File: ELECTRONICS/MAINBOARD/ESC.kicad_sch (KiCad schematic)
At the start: 3 parts, among them U13 STM32G031C6Tx

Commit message: Add files via upload
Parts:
- added J5, J6: Conn_01x05_Socket, Connector_PinHeader_2.54mm:PinHeader_1x05_P2.54mm_Vertical, symbol Connector:Conn_01x05_Socket
- added J7: Conn_01x02_Pin, symbol Connector:Conn_01x02_Pin
- renumbered C35 to C36, C36 to C37, U13 to U17
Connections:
- net +3V3: now also J5.2 (Pin_2), J6.2 (Pin_2)
- net GNDREF: now also J5.3 (Pin_3), J6.3 (Pin_3), J7.2 (Pin_2)
- net MCT8316Z/BRAKE: now also U17.43 (PB4)
- net MCT8316Z/DRVOFF: now also U17.44 (PB5)
- net MCT8316Z/nSCS: now also U17.48 (PB9)
- net AMT_A_R: now reaches U17.11 (PA0)
- net AMT_B_R: now reaches U17.12 (PA1)
- net MCT8316Z1/SDI: now reaches U17.13 (PA2)
- net AMT_X_L: now reaches U17.14 (PA3)
- net MCT8316Z1/nSCS: now reaches U17.15 (PA4)
- net MCT8316Z1/SCLK: now reaches U17.16 (PA5)
- net MCT8316Z1/SDO: now reaches U17.17 (PA6)
- net MCT8316Z1/nSLEEP: now reaches U17.18 (PA7)
- net nFAULT_R: now reaches U17.19 (PB0)
- net FGOUT_R: now reaches U17.20 (PB1)
- net DRVOFF_R: now reaches U17.21 (PB2)
- net BRAKE_R: now reaches U17.22 (PB10)
- net AMT_X_R: now reaches U17.27 (PB15)
- net MCT8316Z1/PWM: now reaches U17.28 (PA8)
- net USART_TX: now reaches U17.29 (USART1_TX/PA9)
- net AMT_A_L: now reaches U17.30 (PC6)
- net AMT_B_L: now reaches U17.31 (PC7)
- net USART_RX: now reaches U17.32 (USART1_RX/PA10)
- net SWDIO: now reaches U17.35 (PA13)
- net SWDIO: now also J6.4 (Pin_4)
- net SWCLK: now reaches U17.36 (PA14)
- net SWCLK: now also J6.5 (Pin_5)
- net FGOUT_L: now reaches U17.39 (PD1)
- net nFAULT_L: now reaches U17.40 (PD2)
- net nSLEEP_L: now reaches U17.41 (PD3)
- net MCT_L_PWM: now reaches U17.42 (PB3)
- net MCT8316Z/SDI: now reaches U17.45 (PB6)
- net MCT8316Z/SDO: now reaches U17.46 (PB7)
- net MCT8316Z/SCLK: now reaches U17.47 (PB8)
- net PF0 renamed nRESET
- new net +24V: J7.1 (Pin_1)
- new net NRESET: J5.5 (Pin_5)
- no-connect marks 0 -> 11
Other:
- sheet MCT8316Z ports: added SCLK, SDI, SDO; removed none
- sheet MCT8316Z1 ports: added 24V, BRAKE, DRVOFF, FGOUT, PWM, SCLK, SDI, SDO, nFAULT, nSCS, nSLEEP; removed none
- note added: "SWIM NC"

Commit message: Add files via upload
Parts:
- removed J7: Conn_01x02_Pin, symbol Connector:Conn_01x02_Pin
- added J4: Conn_01x02_Socket, symbol Connector:Conn_01x02_Socket
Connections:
- net USART_RX: now also J4.1 (Pin_1)
- net USART_TX: now also J4.2 (Pin_2)
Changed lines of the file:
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@@
-	)
-	(junction
-		(at 198.12 26.67)
-		(diameter 0)
-		(color 0 0 0 0)
 	)
 	(junction
@@
 	(wire
 		(pts
-			(xy 171.45 29.21) (xy 168.91 29.21)
-		)
-		(stroke
-			(width 0)
-			(type default)
-		)
-	)
-	(wire
-		(pts
 			(xy 149.86 93.98) (xy 161.29 93.98)
 		)
@@
 	(wire
 		(pts
+			(xy 78.74 83.82) (xy 78.74 87.63)
+		)
+		(stroke
+			(width 0)
+			(type default)
+		)
+	)
+	(wire
+		(pts
 			(xy 107.95 55.88) (xy 114.3 55.88)
 		)
@@
 	(wire
 		(pts
+			(xy 78.74 93.98) (xy 88.9 93.98)
+		)
+		(stroke
+			(width 0)
+			(type default)
+		)
+	)
+	(wire
+		(pts
 			(xy 149.86 99.06) (xy 162.56 99.06)
 		)
@@
 	(wire
 		(pts
+			(xy 78.74 83.82) (xy 88.9 83.82)
+		)
+		(stroke
+			(width 0)
+			(type default)
+		)
+	)
+	(wire
+		(pts
 			(xy 149.86 96.52) (xy 162.56 96.52)
 		)
@@
 	(wire
 		(pts
+			(xy 72.39 90.17) (xy 78.74 90.17)
+		)
+		(stroke
+			(width 0)
+			(type default)
+		)
+	)
+	(wire
+		(pts
 			(xy 149.86 68.58) (xy 162.56 68.58)
 		)
@@
 	(wire
 		(pts
+			(xy 78.74 93.98) (xy 78.74 90.17)
+		)
+		(stroke
+			(width 0)
+			(type default)
+		)
+	)
+	(wire
+		(pts
 			(xy 180.34 63.5) (xy 189.23 63.5)
 		)
@@
 	(wire
 		(pts
-			(xy 168.91 26.67) (xy 198.12 26.67)
+			(xy 78.74 87.63) (xy 72.39 87.63)
 		)
 		(stroke
@@
 		)
 	)
+	(label "USART_RX"
+		(at 88.9 93.98 180)
+		(effects
+			(font
+				(size 1.27 1.27)
+			)
+			(justify right bottom)
+		)
+	)
 	(label "nRESET"
 		(at 105.41 58.42 0)
@@
 		)
 	)
-	(label "PWM_L"
+	(label "MCT_L_PWM"
 		(at 190.5 101.6 180)
 		(effects
@@
 	(label "USART_TX"
 		(at 161.29 71.12 180)
+		(effects
+			(font
+				(size 1.27 1.27)
+			)
+			(justify right bottom)
+		)
+	)
+	(label "USART_TX"
+		(at 88.9 83.82 180)
 		(effects
 			(font
@@
 		)
 	)
+	(hierarchical_label "USART_RX"
+		(shape input)
+		(at 78.74 90.17 0)
+		(effects
+			(font
+				(size 1.27 1.27)
+			)
+			(justify left)
+		)
+	)
 	(hierarchical_label "AMT_B_L"
 		(shape output)
@@
 			)
 			(justify left)
+		)
+	)
+	(hierarchical_label "USART_TX"
+		(shape output)
+		(at 78.74 87.63 0)
+		(effects
+			(font
+				(size 1.27 1.27)
+			)
+			(justify left)
+		)
+	)
+	(hierarchical_label "24V"
+		(shape input)
+		(at 198.12 26.67 180)
+		(effects
+			(font
+				(size 1.27 1.27)
+			)
+			(justify right)
 		)
 	)
@@
 	)
 	(symbol
-		(lib_id "Connector:Conn_01x02_Pin")
-		(at 163.83 26.67 0)
-		(unit 1)
-		(body_style 1)
-		(exclude_from_sim no)
-		(in_bom yes)
-		(on_board yes)
-		(in_pos_files yes)
-		(dnp no)
-		(fields_autoplaced yes)
-		(property "Reference" "J7"
-			(at 164.465 21.59 0)
-			(show_name no)
-			(do_not_autoplace no)
-			(effects
-				(font
-					(size 1.27 1.27)
-				)
-			)
-		)
-		(property "Value" "Conn_01x02_Pin"
-			(at 164.465 24.13 0)
-			(show_name no)
-			(do_not_autoplace no)
-			(effects
-				(font
-					(size 1.27 1.27)
-				)
-			)
-		)
-		(property "Footprint" ""
-			(at 163.83 26.67 0)
-			(hide yes)
-			(show_name no)
-			(do_not_autoplace no)
-			(effects
-				(font
-					(size 1.27 1.27)
-				)
-			)
-		)
-		(property "Datasheet" ""
-			(at 163.83 26.67 0)
-			(hide yes)
-			(show_name no)
-			(do_not_autoplace no)
-			(effects
-				(font
-					(size 1.27 1.27)
-				)
-			)
-		)
-		(property "Description" "Generic connector, single row, 01x02, script generated"
-			(at 163.83 26.67 0)
-			(hide yes)
-			(show_name no)
-			(do_not_autoplace no)
-			(effects
-				(font
-					(size 1.27 1.27)
-				)
-			)
-		)
-		(pin "1"
-		)
-		(pin "2"
-		)
-		(instances
-			(project "autobot_mainboard"
-				(path "/f053f1d0-b1f5-4f80-9758-8ee1a2d3659d/f3a82e5b-62e6-4c1f-9ee9-6ab064c88bd0"
-					(reference "J7")
-					(unit 1)
-				)
-			)
-		)
-	)
-	(symbol
 		(lib_id "power:GNDREF")
 		(at 99.06 49.53 0)
@@
 	)
 	(symbol
-		(lib_id "power:GNDREF")
-		(at 171.45 29.21 0)
+		(lib_id "Connector:Conn_01x02_Socket")
+		(at 67.31 90.17 180)
 		(unit 1)
 		(body_style 1)
@@
 		(dnp no)
 		(fields_autoplaced yes)
-		(property "Reference" "#PWR060"
-			(at 171.45 35.56 0)
-			(hide yes)
-			(show_name no)
-			(do_not_autoplace no)
-			(effects
-				(font
-					(size 1.27 1.27)
-				)
-			)
-		)
-		(property "Value" "GNDREF"
-			(at 171.45 34.29 0)
-			(hide yes)
+		(property "Reference" "J4"
+			(at 67.945 82.55 0)
+			(show_name no)
+			(do_not_autoplace no)
+			(effects
+				(font
+					(size 1.27 1.27)
+				)
+			)
+		)
+		(property "Value" "Conn_01x02_Socket"
+			(at 67.945 85.09 0)
 			(show_name no)
 			(do_not_autoplace no)
@@
 		)
 		(property "Footprint" ""
-			(at 171.45 29.21 0)
+			(at 67.31 90.17 0)
 			(hide yes)
 			(show_name no)
@@
 		)
 		(property "Datasheet" ""
-			(at 171.45 29.21 0)
-			(hide yes)
-			(show_name no)
-			(do_not_autoplace no)
-			(effects
-				(font
-					(size 1.27 1.27)
-				)
-			)
-		)
-		(property "Description" "Power symbol creates a global label with name \"GNDREF\" , reference supply ground"
-			(at 171.45 29.21 0)
+			(at 67.31 90.17 0)
+			(hide yes)
+			(show_name no)
+			(do_not_autoplace no)
+			(effects
+				(font
+					(size 1.27 1.27)
+				)
+			)
+		)
+		(property "Description" "Generic connector, single row, 01x02, script generated"
+			(at 67.31 90.17 0)
 			(hide yes)
 			(show_name no)
@@
 		)
 		(pin "1"
+		)
+		(pin "2"
 		)
 		(instances
 			(project "autobot_mainboard"
 				(path "/f053f1d0-b1f5-4f80-9758-8ee1a2d3659d/f3a82e5b-62e6-4c1f-9ee9-6ab064c88bd0"
-					(reference "#PWR060")
+					(reference "J4")
 					(unit 1)
 				)

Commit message: Add files via upload
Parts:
- removed J5, J6: Conn_01x05_Socket, Connector_PinHeader_2.54mm:PinHeader_1x05_P2.54mm_Vertical, symbol Connector:Conn_01x05_Socket
- added J20: Conn_02x05_Odd_Even, symbol Connector_Generic:Conn_02x05_Odd_Even
- C36, C37: footprint (none) -> Capacitor_SMD:C_0402_1005Metric
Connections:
- net +3V3: now also J20.7 (Pin_7), J20.8 (Pin_8)
- net GNDREF: now also J20.5 (Pin_5), J20.6 (Pin_6)
- net NRESET: now also J20.1 (Pin_1)
- net SWCLK: now also J20.2 (Pin_2)
- net SWDIO: now also J20.4 (Pin_4)

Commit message: Add files via upload
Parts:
- J20: footprint (none) -> Connector_PinSocket_2.54mm:PinSocket_2x05_P2.54mm_Vertical
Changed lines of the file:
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@@
 			)
 		)
-		(property "Footprint" ""
+		(property "Footprint" "Connector_PinSocket_2.54mm:PinSocket_2x05_P2.54mm_Vertical"
 			(at 69.85 111.76 0)
 			(hide yes)

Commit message: commit 1 commit 1 10/03/2026
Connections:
- net AMT_A_L: no longer U17.30 (PC6)
- net AMT_A_R: no longer U17.11 (PA0)
- net AMT_B_L: no longer U17.31 (PC7)
- net AMT_B_R: no longer U17.12 (PA1)
- net AMT_X_L: no longer U17.14 (PA3)
- net BRAKE_R: no longer U17.22 (PB10)
- net DRVOFF_R: no longer U17.21 (PB2)
- net USART_RX: now also U17.34 (PA10/PA12); no longer U17.32 (USART1_RX/PA10)
- net USART_TX: now also U17.33 (PA9/PA11); no longer U17.29 (USART1_TX/PA9)
- net nFAULT_R: no longer U17.19 (PB0)
- net SDA_R: now reaches U17.26 (PB14)
- net AMT_X_R: no longer names the net of U17.27 (PB15)
- net FGOUT_L: no longer names the net of U17.39 (PD1)
- net FGOUT_R: no longer names the net of U17.20 (PB1)
- net MCT8316Z/BRAKE: no longer names the net of U17.43 (PB4)
- net MCT8316Z/DRVOFF: no longer names the net of U17.44 (PB5)
- net MCT8316Z/SCLK renamed SCL
- net MCT8316Z/SDI: no longer names the net of U17.45 (PB6)
- net MCT8316Z/SDO: no longer names the net of U17.46 (PB7)
- net MCT8316Z/nSCS renamed SDA
- net MCT8316Z1/PWM: no longer names the net of U17.28 (PA8)
- net MCT8316Z1/SCLK: no longer names the net of U17.16 (PA5)
- net MCT8316Z1/SDI: no longer names the net of U17.13 (PA2)
- net MCT8316Z1/SDO: no longer names the net of U17.17 (PA6)
- net MCT8316Z1/nSCS: no longer names the net of U17.15 (PA4)
- net MCT8316Z1/nSLEEP: no longer names the net of U17.18 (PA7)
- net MCT_L_PWM: no longer names the net of U17.42 (PB3)
- net nFAULT_L: no longer names the net of U17.40 (PD2)
- net nSLEEP_L: no longer names the net of U17.41 (PD3)
- new net SCL_R: U17.22 (PB10)
- no-connect marks 11 -> 6
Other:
- removed sheet MCT8316Z
- removed sheet MCT8316Z1
- added sheet MCT8316A1V (MCT8316A1V.kicad_sch)
- added sheet MCT8316A1V1 (MCT8316A1V.kicad_sch)

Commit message: driver board schematic
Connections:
- net AMT_A_L: now also U17.11 (PA0)
- net AMT_A_R: now also U17.30 (PC6)
- net AMT_B_L: now also U17.12 (PA1)
- net AMT_B_R: now also U17.31 (PC7)
- net AMT_X_L: now also U17.13 (PA2), U17.28 (PA8)
- net BRAKE: now also U17.39 (PD1)
- net BRAKE_R: now also U17.25 (PB13)
- net DACOUT1: now also U17.41 (PD3)
- net DACOUT1_R: now also U17.16 (PA5)
- net DACOUT2: now also U17.40 (PD2)
- net DACOUT2_R: now also U17.17 (PA6)
- net DIR: now also U17.44 (PB5)
- net DIR_R: now also U17.19 (PB0)
- net DRVOFF: now also U17.43 (PB4)
- net DRVOFF_R: now also U17.24 (PB12)
- net EXT_WD: now also U17.38 (PD0)
- net EXT_WD_R: now also U17.20 (PB1)
- net FG: now also U17.46 (PB7)
- net FG_R: now also U17.21 (PB2)
- net PWM: now also U17.45 (PB6)
- net PWM_R: now also U17.18 (PA7)
- net nFAULT: now also U17.42 (PB3)
- net nFAULT_R: now also U17.23 (PB11)

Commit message: 10/3 final
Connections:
- net BRAKE_R: now also U17.18 (PA7); no longer U17.25 (PB13)
- net DACOUT1_R: now also U17.17 (PA6); no longer U17.16 (PA5)
- net DACOUT2_R: now also U17.16 (PA5); no longer U17.17 (PA6)
- net PWM_R: now also U17.15 (PA4); no longer U17.18 (PA7)
- net SCL_R: now also U17.25 (PB13); no longer U17.22 (PB10)

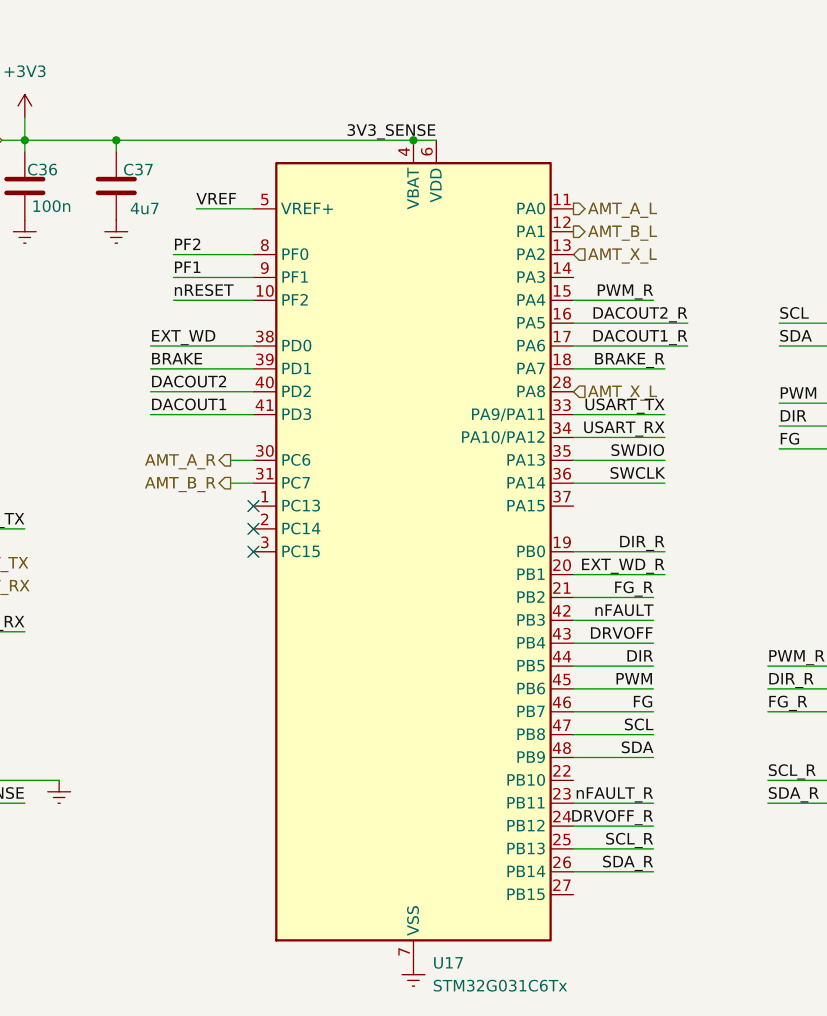
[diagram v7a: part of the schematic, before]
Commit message: new stm32 footprint
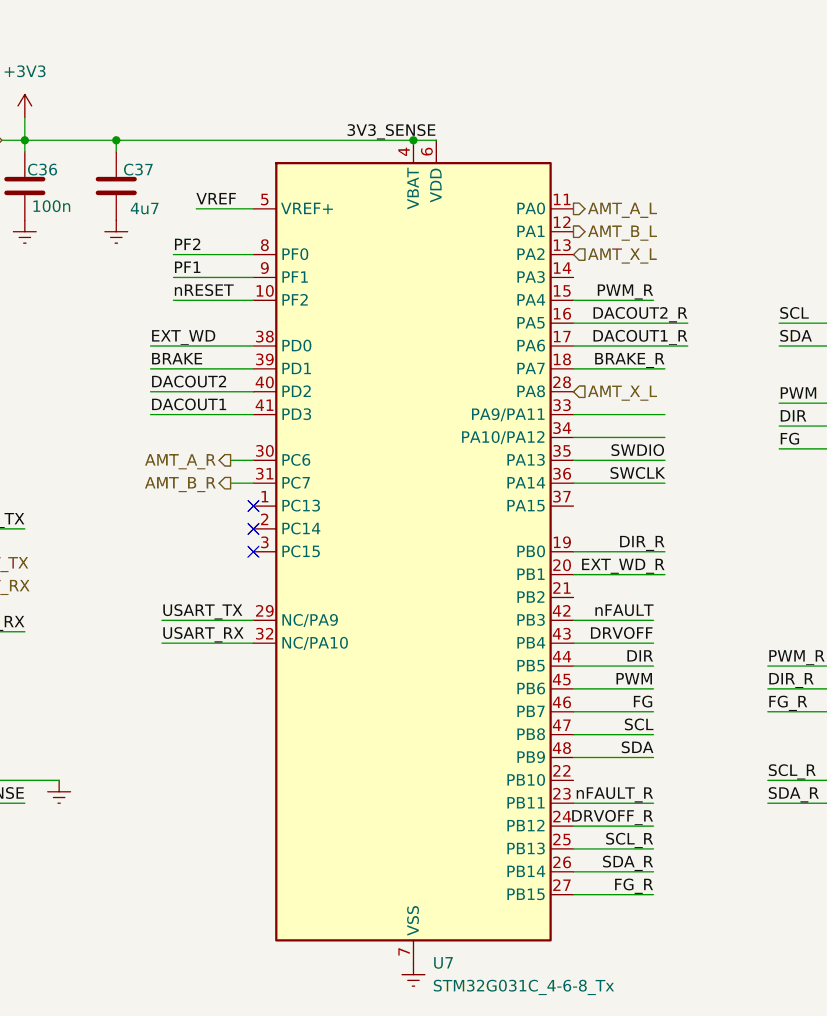
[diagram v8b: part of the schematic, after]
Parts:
- removed U17: STM32G031C6Tx, Package_QFP:LQFP-48_7x7mm_P0.5mm, symbol MCU_ST_STM32G0:STM32G031C6Tx
- added U7: STM32G031C_4-6-8_Tx, Package_QFP:LQFP-48_7x7mm_P0.5mm, symbol AutoBotLibrary:STM32G031C_4-6-8_Tx
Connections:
- net +3V3: now also U7.4 (VBAT), U7.6 (VDD)
- net AMT_A_L: now also U7.11 (PA0)
- net AMT_A_R: now also U7.30 (PC6)
- net AMT_B_L: now also U7.12 (PA1)
- net AMT_B_R: now also U7.31 (PC7)
- net AMT_X_L: now also U7.13 (PA2), U7.28 (PA8)
- net BRAKE: now also U7.39 (PD1)
- net BRAKE_R: now also U7.18 (PA7)
- net DACOUT1: now also U7.41 (PD3)
- net DACOUT1_R: now also U7.17 (PA6)
- net DACOUT2: now also U7.40 (PD2)
- net DACOUT2_R: now also U7.16 (PA5)
- net DIR: now also U7.44 (PB5)
- net DIR_R: now also U7.19 (PB0)
- net DRVOFF: now also U7.43 (PB4)
- net DRVOFF_R: now also U7.24 (PB12)
- net EXT_WD: now also U7.38 (PD0)
- net EXT_WD_R: now also U7.20 (PB1)
- net FG: now also U7.46 (PB7)
- net FG_R: now also U7.27 (PB15)
- net GNDREF: now also U7.7 (VSS)
- net PF1: now also U7.9 (PF1)
- net PF2: now also U7.8 (PF0)
- net PWM: now also U7.45 (PB6)
- net PWM_R: now also U7.15 (PA4)
- net SCL: now also U7.47 (PB8)
- net SCL_R: now also U7.25 (PB13)
- net SDA: now also U7.48 (PB9)
- net SDA_R: now also U7.26 (PB14)
- net SWCLK: now also U7.36 (PA14)
- net SWDIO: now also U7.35 (PA13)
- net USART_RX: now also U7.32 (NC/PA10)
- net USART_TX: now also U7.29 (NC/PA9)
- net VREF: now also U7.5 (VREF+)
- net nFAULT: now also U7.42 (PB3)
- net nFAULT_R: now also U7.23 (PB11)
- net nRESET: now also U7.10 (PF2)
